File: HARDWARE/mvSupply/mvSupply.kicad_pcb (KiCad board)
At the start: 2 copper layers, 169.3 x 128 mm, 4 parts

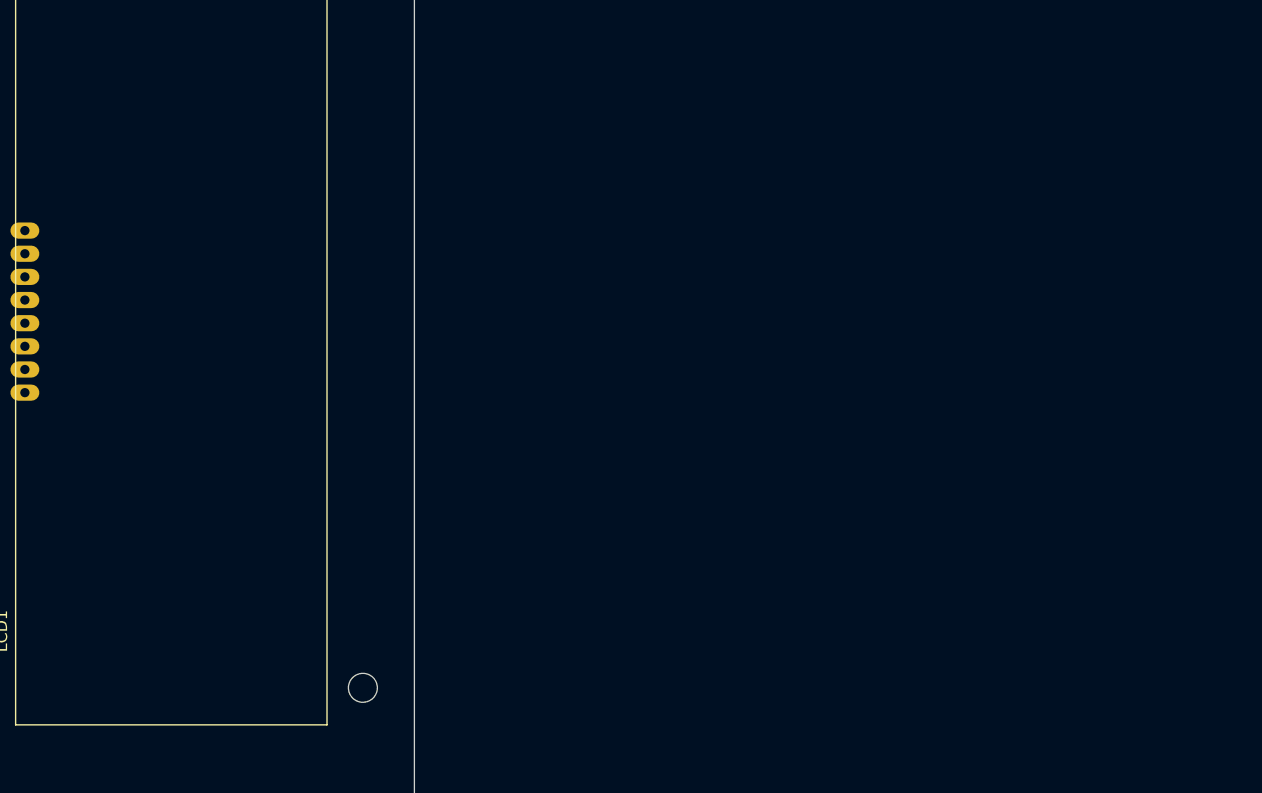
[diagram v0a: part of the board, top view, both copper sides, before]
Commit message: Testing submodule retrieval
Committing to see if it will grab latest library commit
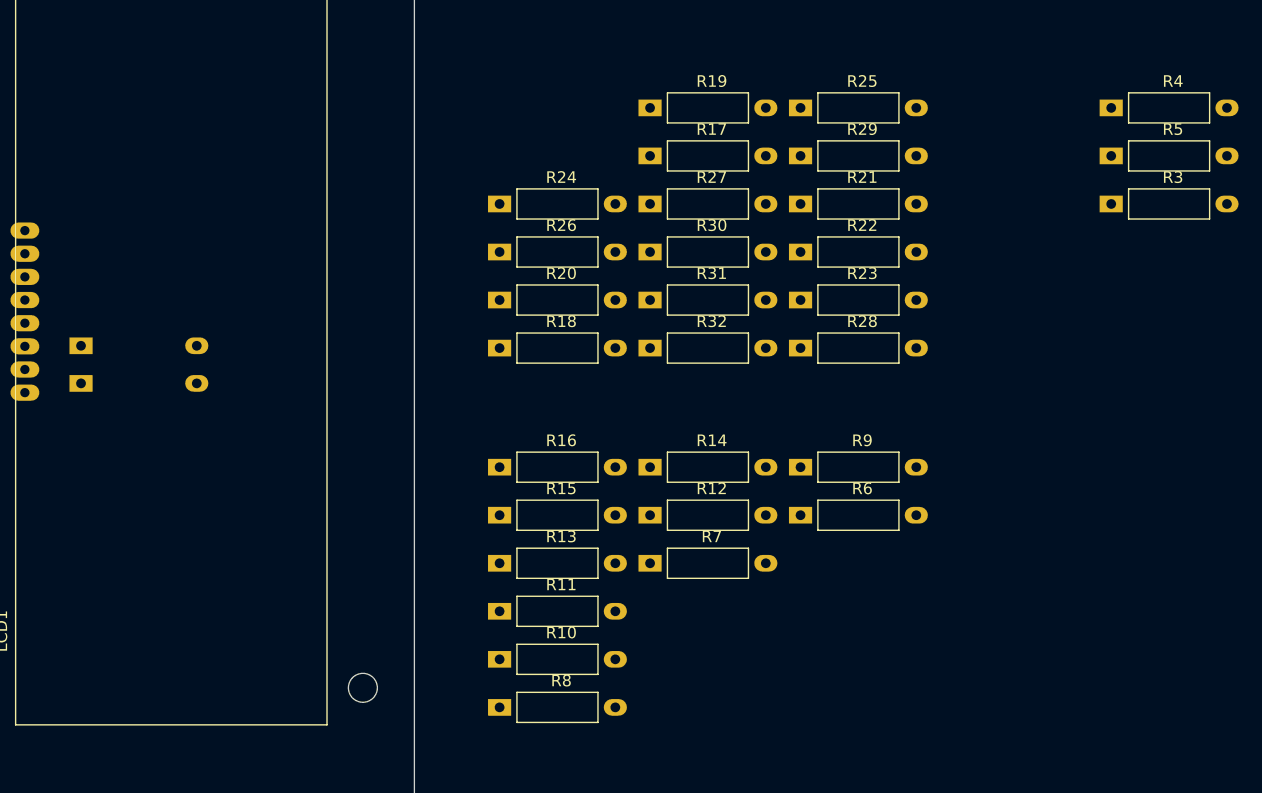
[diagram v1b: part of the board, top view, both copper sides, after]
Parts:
- added R10: R, master-vampire:R_AXIAL_L7mm_D2.6mm_P10mm_Horizontal, F.Cu at (222.7, 95.1)
- added R11: R, master-vampire:R_AXIAL_L7mm_D2.6mm_P10mm_Horizontal, F.Cu at (222.7, 90.9)
- added R12: R, master-vampire:R_AXIAL_L7mm_D2.6mm_P10mm_Horizontal, F.Cu at (235.7, 82.6)
- added R13: R, master-vampire:R_AXIAL_L7mm_D2.6mm_P10mm_Horizontal, F.Cu at (222.7, 86.8)
- added R14: R, master-vampire:R_AXIAL_L7mm_D2.6mm_P10mm_Horizontal, F.Cu at (235.7, 78.5)
- added R15: R, master-vampire:R_AXIAL_L7mm_D2.6mm_P10mm_Horizontal, F.Cu at (222.7, 82.6)
- added R16: R, master-vampire:R_AXIAL_L7mm_D2.6mm_P10mm_Horizontal, F.Cu at (222.7, 78.5)
- added R17: R, master-vampire:R_AXIAL_L7mm_D2.6mm_P10mm_Horizontal, F.Cu at (235.7, 51.6)
- added R18: R, master-vampire:R_AXIAL_L7mm_D2.6mm_P10mm_Horizontal, F.Cu at (222.7, 68.2)
- added R19: R, master-vampire:R_AXIAL_L7mm_D2.6mm_P10mm_Horizontal, F.Cu at (235.7, 47.5)
- added R20: R, master-vampire:R_AXIAL_L7mm_D2.6mm_P10mm_Horizontal, F.Cu at (222.7, 64.0)
- added R21: R, master-vampire:R_AXIAL_L7mm_D2.6mm_P10mm_Horizontal, F.Cu at (248.7, 55.8)
- added R22: R, master-vampire:R_AXIAL_L7mm_D2.6mm_P10mm_Horizontal, F.Cu at (248.7, 59.9)
- added R23: R, master-vampire:R_AXIAL_L7mm_D2.6mm_P10mm_Horizontal, F.Cu at (248.7, 64.0)
- added R24: R, master-vampire:R_AXIAL_L7mm_D2.6mm_P10mm_Horizontal, F.Cu at (222.7, 55.8)
- added R25: R, master-vampire:R_AXIAL_L7mm_D2.6mm_P10mm_Horizontal, F.Cu at (248.7, 47.5)
- added R26: R, master-vampire:R_AXIAL_L7mm_D2.6mm_P10mm_Horizontal, F.Cu at (222.7, 59.9)
- added R27: R, master-vampire:R_AXIAL_L7mm_D2.6mm_P10mm_Horizontal, F.Cu at (235.7, 55.8)
- added R28: R, master-vampire:R_AXIAL_L7mm_D2.6mm_P10mm_Horizontal, F.Cu at (248.7, 68.2)
- added R29: R, master-vampire:R_AXIAL_L7mm_D2.6mm_P10mm_Horizontal, F.Cu at (248.7, 51.6)
- added R3: R, master-vampire:R_AXIAL_L7mm_D2.6mm_P10mm_Horizontal, F.Cu at (275.5, 55.8)
- added R30: R, master-vampire:R_AXIAL_L7mm_D2.6mm_P10mm_Horizontal, F.Cu at (235.7, 59.9)
- added R31: R, master-vampire:R_AXIAL_L7mm_D2.6mm_P10mm_Horizontal, F.Cu at (235.7, 64.0)
- added R32: R, master-vampire:R_AXIAL_L7mm_D2.6mm_P10mm_Horizontal, F.Cu at (235.7, 68.2)
- added R33: R, master-vampire:R_AXIAL_L7mm_D2.6mm_P10mm_Horizontal, B.Cu at (186.5, 68.0)
- added R34: R, master-vampire:R_AXIAL_L7mm_D2.6mm_P10mm_Horizontal, B.Cu at (186.5, 71.2)
- added R4: R, master-vampire:R_AXIAL_L7mm_D2.6mm_P10mm_Horizontal, F.Cu at (275.5, 47.5)
- added R5: R, master-vampire:R_AXIAL_L7mm_D2.6mm_P10mm_Horizontal, F.Cu at (275.5, 51.6)
- added R6: R, master-vampire:R_AXIAL_L7mm_D2.6mm_P10mm_Horizontal, F.Cu at (248.7, 82.6)
- added R7: R, master-vampire:R_AXIAL_L7mm_D2.6mm_P10mm_Horizontal, F.Cu at (235.7, 86.8)
- added R8: R, master-vampire:R_AXIAL_L7mm_D2.6mm_P10mm_Horizontal, F.Cu at (222.7, 99.2)
- added R9: R, master-vampire:R_AXIAL_L7mm_D2.6mm_P10mm_Horizontal, F.Cu at (248.7, 78.5)
